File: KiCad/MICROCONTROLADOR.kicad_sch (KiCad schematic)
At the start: 10 parts, among them J1 Screw_Terminal_01x05, SW1 SW_Push, U1 PIC24HJ128GP502, Y1 8 MHz

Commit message: Cambio en la parte de motores y drivers
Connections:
- net MCU_SCL: now reaches U1.17 (TCK/SCL1/RP8/CN22/PMD4/RB8)
- net MCU_SDA: now reaches U1.18 (TDO/SDA1/RP9/CN21/PMD3/RB9)
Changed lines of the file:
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@@
-	(wire
-		(pts
-			(xy 194.31 139.7) (xy 200.66 139.7)
-		)
-		(stroke
-			(width 0)
-			(type default)
-		)
-	)
 	(wire
 		(pts
@@
 	(wire
 		(pts
-			(xy 200.66 139.7) (xy 200.66 140.97)
-		)
-		(stroke
-			(width 0)
-			(type default)
-		)
-	)
-	(wire
-		(pts
 			(xy 69.85 41.91) (xy 69.85 30.48)
 		)
@@
 	(wire
 		(pts
-			(xy 207.01 140.97) (xy 207.01 137.16)
-		)
-		(stroke
-			(width 0)
-			(type default)
-		)
-	)
-	(wire
-		(pts
 			(xy 194.31 58.42) (xy 199.39 58.42)
 		)
@@
 		(pts
 			(xy 62.23 66.04) (xy 62.23 74.93)
-		)
-		(stroke
-			(width 0)
-			(type default)
-		)
-	)
-	(wire
-		(pts
-			(xy 194.31 137.16) (xy 207.01 137.16)
 		)
 		(stroke
@@
 		)
 	)
+	(global_label "MCU_SCL"
+		(shape bidirectional)
+		(at 180.34 96.52 0)
+		(fields_autoplaced yes)
+		(effects
+			(font
+				(size 1.27 1.27)
+			)
+			(justify left)
+		)
+		(property "Intersheetrefs" "${INTERSHEET_REFS}"
+			(at 192.9636 96.52 0)
+			(effects
+				(font
+					(size 1.27 1.27)
+				)
+				(justify left)
+				(hide yes)
+			)
+		)
+	)
 	(global_label "HALL_OUT"
 		(shape output)
@@
 		(property "Intersheetrefs" "${INTERSHEET_REFS}"
 			(at 88.0147 36.83 0)
+			(effects
+				(font
+					(size 1.27 1.27)
+				)
+				(justify left)
+				(hide yes)
+			)
+		)
+	)
+	(global_label "MCU_SDA"
+		(shape bidirectional)
+		(at 180.34 91.44 0)
+		(fields_autoplaced yes)
+		(effects
+			(font
+				(size 1.27 1.27)
+			)
+			(justify left)
+		)
+		(property "Intersheetrefs" "${INTERSHEET_REFS}"
+			(at 193.0241 91.44 0)
 			(effects
 				(font
@@
 				)
 			)
+			(project "SEIENTS_EDD"
+				(path "/b6401b4f-5426-49b8-bb2e-8ecdb19989ef/2352108e-71c7-4bd2-90ee-aa6ba1d65197"
+					(reference "R?")
+					(unit 1)
+				)
+			)
 		)
 	)
@@
 				)
 			)
+			(project "SEIENTS_EDD"
+				(path "/b6401b4f-5426-49b8-bb2e-8ecdb19989ef/2352108e-71c7-4bd2-90ee-aa6ba1d65197"
+					(reference "#PWR?")
+					(unit 1)
+				)
+			)
 		)
 	)
@@
 				)
 			)
+			(project "SEIENTS_EDD"
+				(path "/b6401b4f-5426-49b8-bb2e-8ecdb19989ef/2352108e-71c7-4bd2-90ee-aa6ba1d65197"
+					(reference "C?")
+					(unit 1)
+				)
+			)
 		)
 	)
@@
 				)
 			)
+			(project "SEIENTS_EDD"
+				(path "/b6401b4f-5426-49b8-bb2e-8ecdb19989ef/2352108e-71c7-4bd2-90ee-aa6ba1d65197"
+					(reference "#PWR?")
+					(unit 1)
+				)
+			)
 		)
 	)
@@
 				(path "/9b2329e0-99c8-4c5f-bbda-c735127483a8"
 					(reference "#PWR06")
+					(unit 1)
+				)
+			)
+			(project "SEIENTS_EDD"
+				(path "/b6401b4f-5426-49b8-bb2e-8ecdb19989ef/2352108e-71c7-4bd2-90ee-aa6ba1d65197"
+					(reference "#PWR?")
 					(unit 1)
 				)
@@
 				)
 			)
+			(project "SEIENTS_EDD"
+				(path "/b6401b4f-5426-49b8-bb2e-8ecdb19989ef/2352108e-71c7-4bd2-90ee-aa6ba1d65197"
+					(reference "C?")
+					(unit 1)
+				)
+			)
 		)
 	)
@@
 				)
 			)
+			(project "SEIENTS_EDD"
+				(path "/b6401b4f-5426-49b8-bb2e-8ecdb19989ef/2352108e-71c7-4bd2-90ee-aa6ba1d65197"
+					(reference "#PWR?")
+					(unit 1)
+				)
+			)
 		)
 	)
@@
 				(path "/9b2329e0-99c8-4c5f-bbda-c735127483a8"
 					(reference "#PWR07")
+					(unit 1)
+				)
+			)
+			(project "SEIENTS_EDD"
+				(path "/b6401b4f-5426-49b8-bb2e-8ecdb19989ef/2352108e-71c7-4bd2-90ee-aa6ba1d65197"
+					(reference "#PWR?")
 					(unit 1)
 				)
@@
 				)
 			)
+			(project "SEIENTS_EDD"
+				(path "/b6401b4f-5426-49b8-bb2e-8ecdb19989ef/2352108e-71c7-4bd2-90ee-aa6ba1d65197"
+					(reference "SW?")
+					(unit 1)
+				)
+			)
 		)
 	)
@@
 				)
 			)
+			(project "SEIENTS_EDD"
+				(path "/b6401b4f-5426-49b8-bb2e-8ecdb19989ef/2352108e-71c7-4bd2-90ee-aa6ba1d65197"
+					(reference "U?")
+					(unit 1)
+				)
+			)
 		)
 	)
@@
 					(unit 1)
 				)
+			)
+			(project "SEIENTS_EDD"
+				(path "/b6401b4f-5426-49b8-bb2e-8ecdb19989ef/2352108e-71c7-4bd2-90ee-aa6ba1d65197"
+					(reference "C?")
+					(unit 1)
+				)

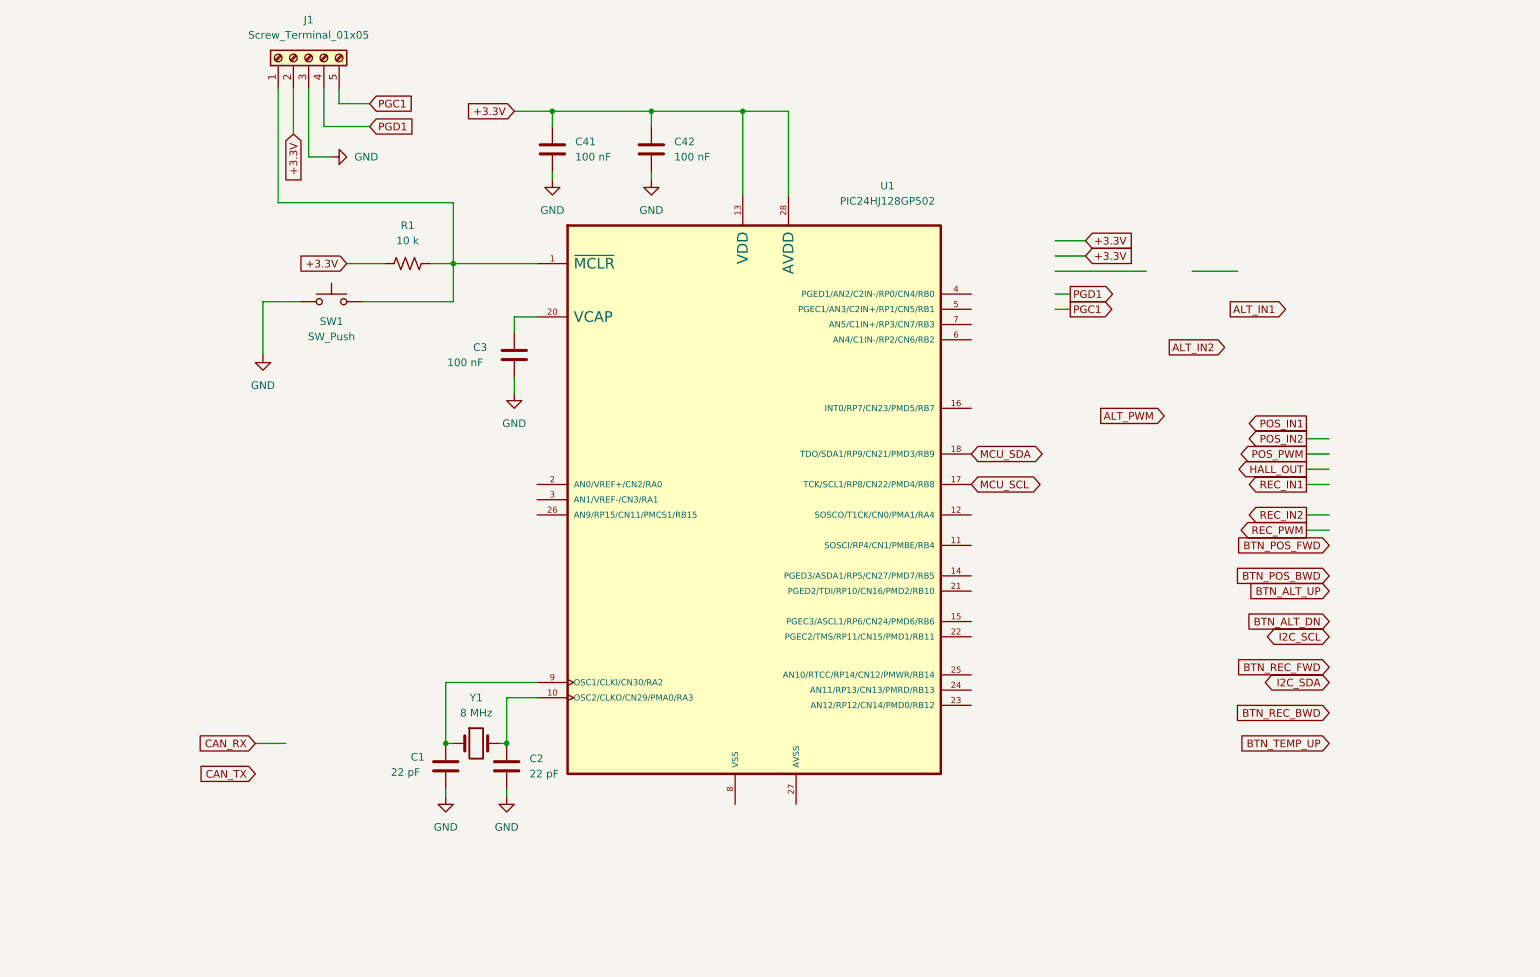
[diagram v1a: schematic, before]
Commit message: Modificacions al MICROCONTROLADOR
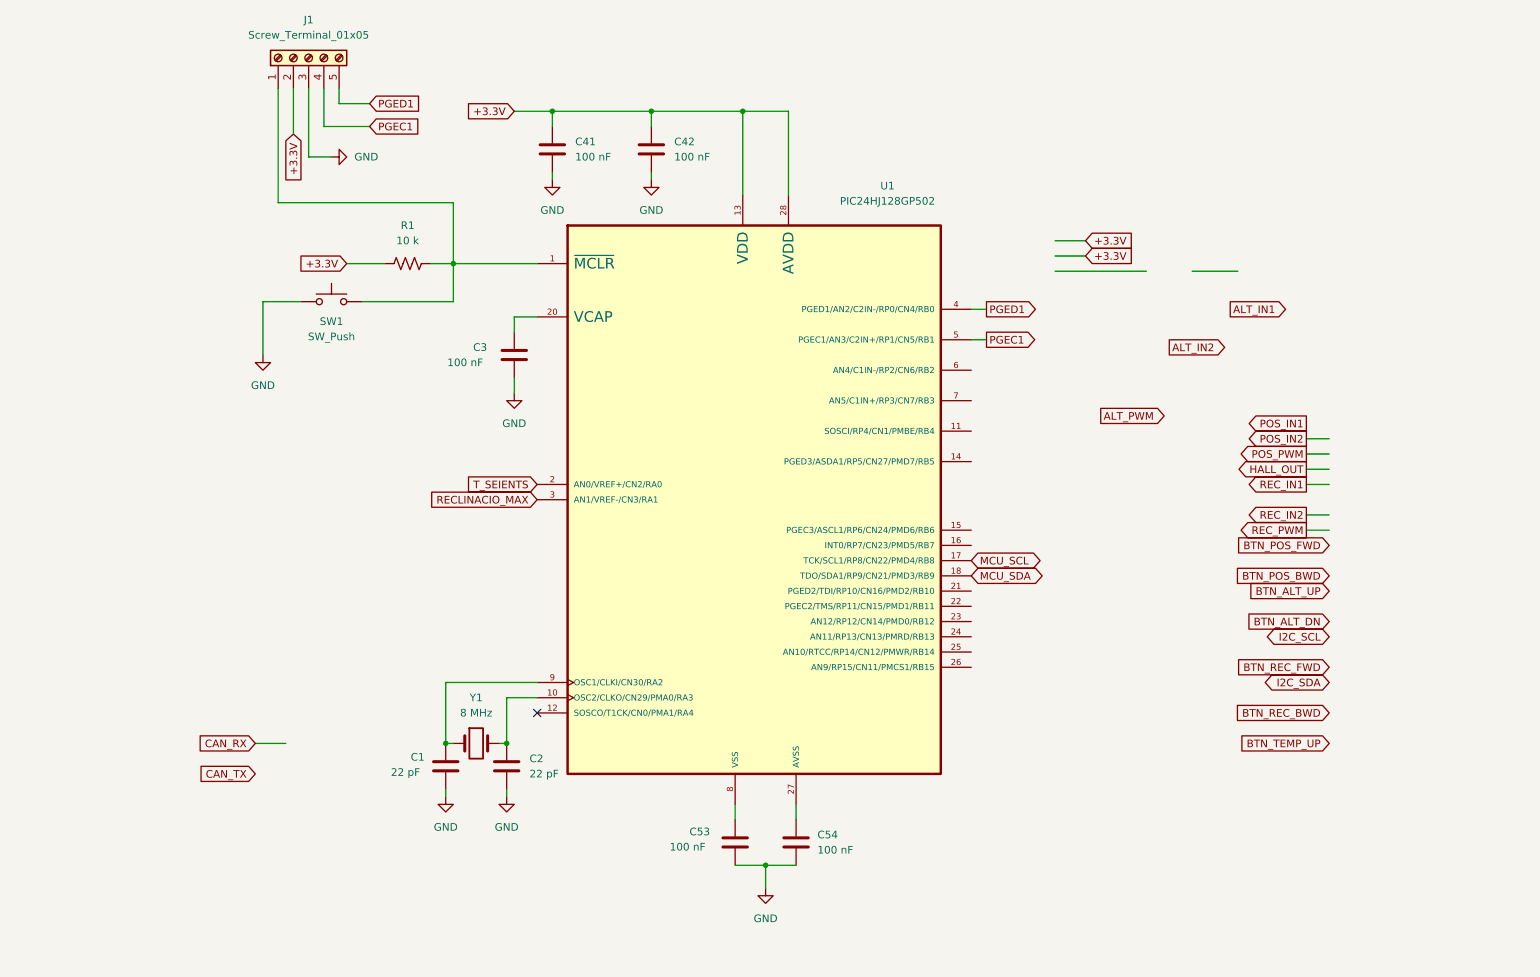
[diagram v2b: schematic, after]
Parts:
- added C53, C54: 100 nF, symbol Device:C
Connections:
- net PGC1 is gone; now on net PGED1: J1.5 (Pin_5)
- net PGD1 is gone; now on net PGEC1: J1.4 (Pin_4)
- net GND: now also C53.2, C54.2
- net T_SEIENTS: now reaches U1.2 (AN0/VREF+/CN2/RA0)
- net at U1.27 (AVSS): now also C54.1
- net RECLINACIO_MAX: now reaches U1.3 (AN1/VREF-/CN3/RA1)
- net PGED1: now reaches U1.4 (PGED1/AN2/C2IN-/RP0/CN4/RB0)
- net PGEC1: now reaches U1.5 (PGEC1/AN3/C2IN+/RP1/CN5/RB1)
- net at U1.8 (VSS): now also C53.1
- no-connect marks 0 -> 1

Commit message: Modificacions al MICROCONTROLADOR
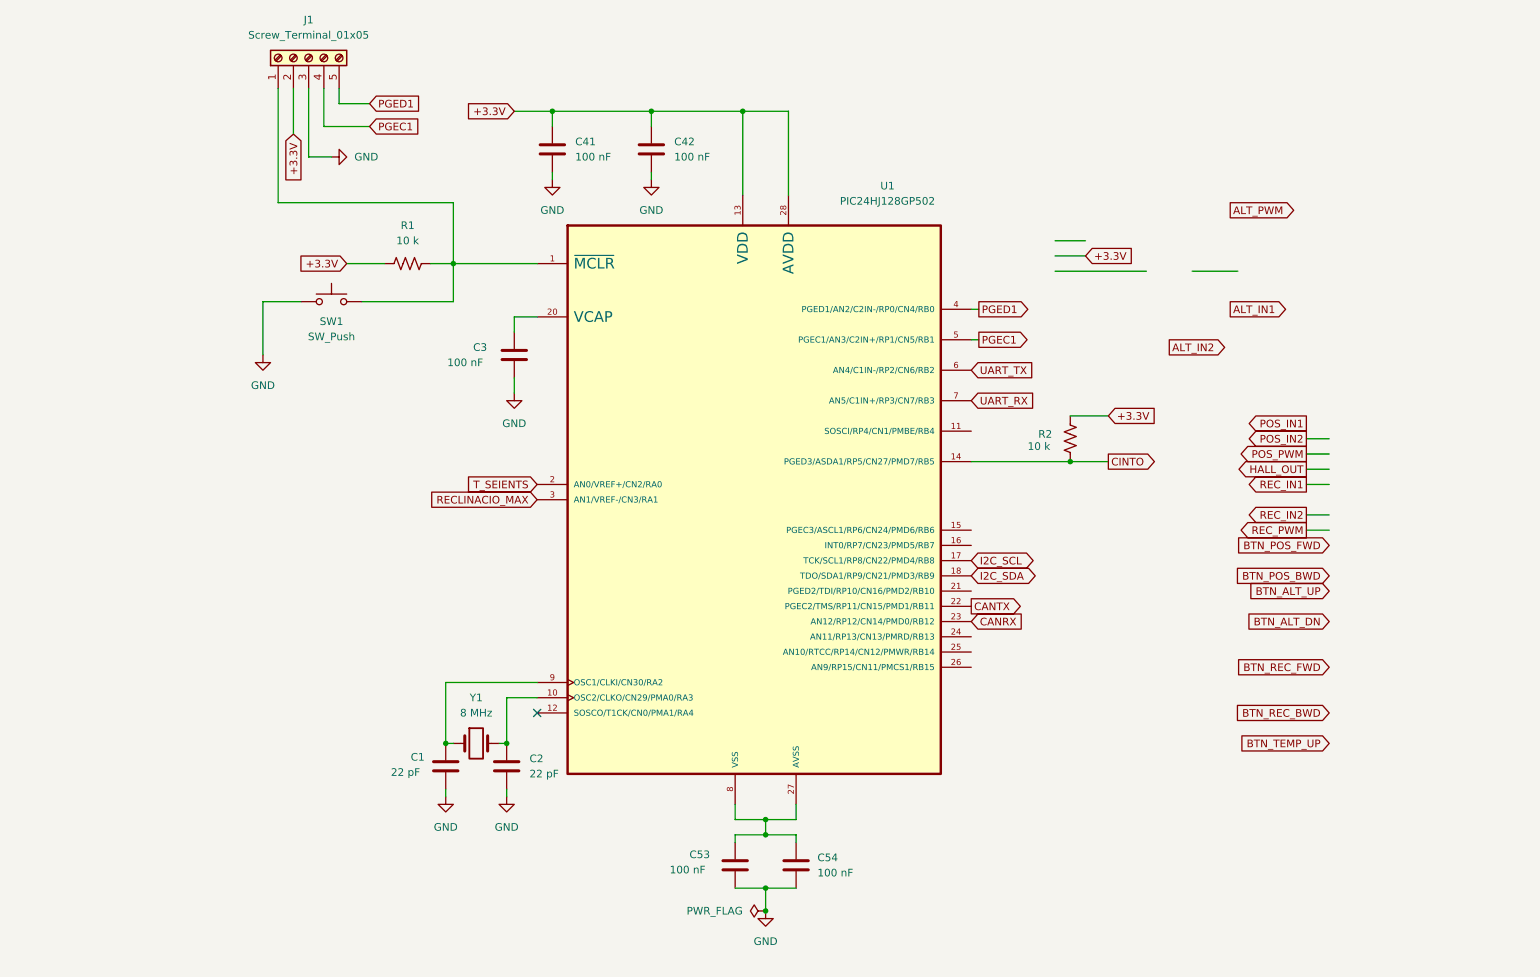
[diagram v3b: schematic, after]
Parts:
- added R2: 10 k, symbol Device:R_US
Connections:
- net MCU_SCL is gone; now on net I2C_SCL: U1.17 (TCK/SCL1/RP8/CN22/PMD4/RB8)
- net MCU_SDA is gone; now on net I2C_SDA: U1.18 (TDO/SDA1/RP9/CN21/PMD3/RB9)
- net +3.3V: now also R2.2
- net at C54.1, U1.27 (AVSS): now also C53.1, U1.8 (VSS)
- net CINTO: now reaches U1.14 (PGED3/ASDA1/RP5/CN27/PMD7/RB5)
- net CINTO: now also R2.1
- net CANTX: now reaches U1.22 (PGEC2/TMS/RP11/CN15/PMD1/RB11)
- net CANRX: now reaches U1.23 (AN12/RP12/CN14/PMD0/RB12)
- net UART_TX: now reaches U1.6 (AN4/C1IN-/RP2/CN6/RB2)
- net UART_RX: now reaches U1.7 (AN5/C1IN+/RP3/CN7/RB3)
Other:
- moved on the sheet: C53, C54

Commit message: Modificacions al MOSFET
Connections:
- net CALEFACCIÓ: now reaches U1.26 (AN9/RP15/CN11/PMCS1/RB15)
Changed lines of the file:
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@@
+		)
+	)
+	(global_label "CALEFACCIÓ"
+		(shape output)
+		(at 180.34 127 0)
+		(fields_autoplaced yes)
+		(effects
+			(font
+				(size 1.27 1.27)
+			)
+			(justify left)
+		)
+		(property "Intersheetrefs" "${INTERSHEET_REFS}"
+			(at 194.5134 127 0)
+			(effects
+				(font
+					(size 1.27 1.27)
+				)
+				(justify left)
+				(hide yes)
+			)
 		)
 	)
